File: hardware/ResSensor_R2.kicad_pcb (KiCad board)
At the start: 2 copper layers, 36.9 x 17 mm, 33 parts, among them J1 Conn_01x02, J2 Conn_01x04, U1 SPX3819M5-L-3-3, U2 STM32G030F6Px, U3 nRF24L01P, U4 CS1237, Y1 16MHz

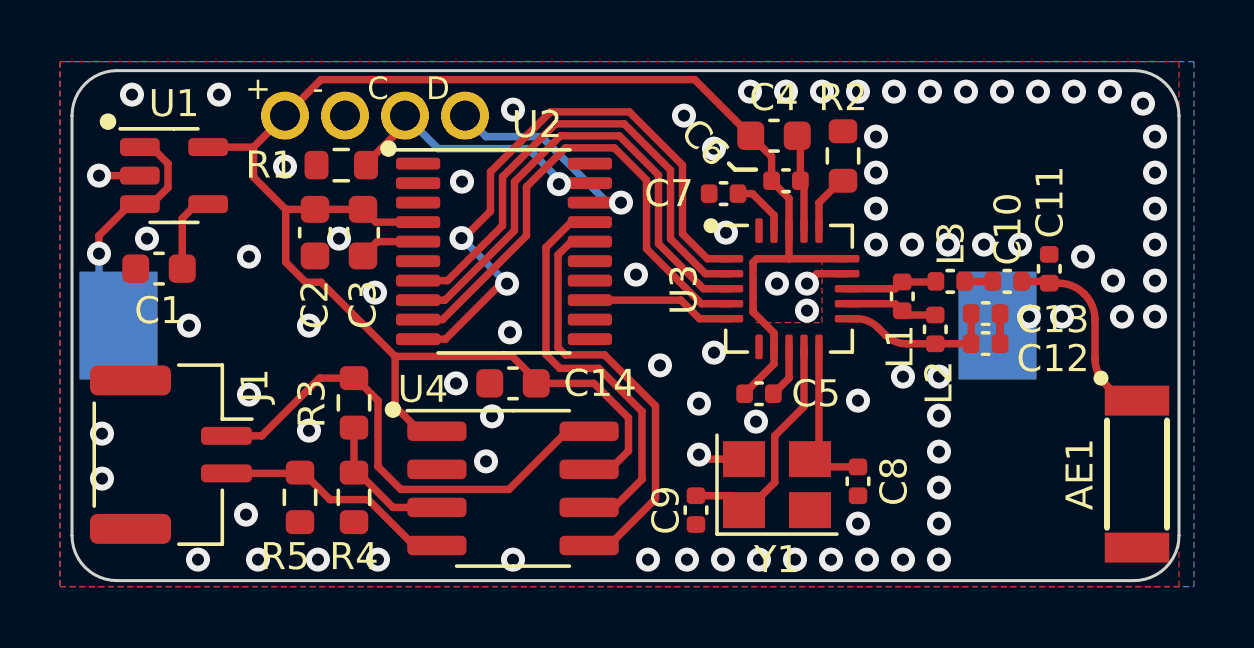
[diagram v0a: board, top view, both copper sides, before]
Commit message: Revise hardware, adding indicator LED
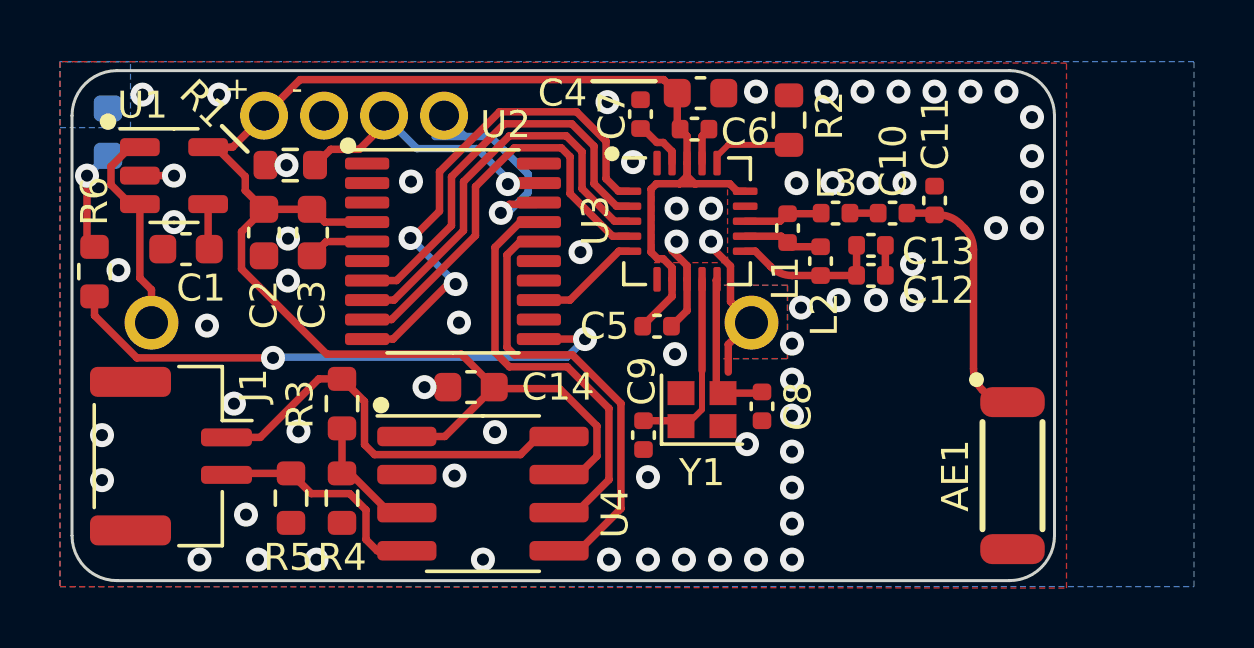
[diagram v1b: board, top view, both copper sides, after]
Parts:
- added D1: Yellow, LED_SMD:LED_0603_1608Metric, B.Cu at (20.4, 20.1)
- added R6: 2k TBD, Resistor_SMD:R_0603_1608Metric, F.Cu at (19.9, 24.7)
- BT1: footprint Battery:BatteryHolder_Keystone_1060_1x2032 -> ResSensor_footprints:BatteryHolder_2032_THT_P20
- Y1: footprint Crystal:Crystal_SMD_3225-4Pin_3.2x2.5mm -> Crystal:Crystal_SMD_2016-4Pin_2.0x1.6mm
- moved C11 4.45 mm to (48.0, 22.3)
- moved C12 4.45 mm to (45.8, 24.8)
- moved C13 4.45 mm to (45.8, 23.8)
- moved C10 4.45 mm to (46.6, 22.8)
- moved L1 4.45 mm to (43.1, 23.2)
- moved L2 4.45 mm to (44.2, 24.4)
- moved L3 4.45 mm to (44.7, 22.8)
- moved AE1 4.15 mm to (50.5, 31.5)
- moved C5 4.08 mm to (38.7, 26.5)
- moved U3 4.08 mm to (39.7, 23.0)
- moved C8 4.06 mm to (42.2, 29.2)
- moved C7 3.83 mm to (38.1, 19.4), turned to 90 degrees
- moved G*** 3.70 mm to (45.5, 32.7)
- moved G*** 3.70 mm to (45.7, 20.4)
- moved Y1 3.54 mm to (40.2, 29.3)
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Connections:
- U2 pad 11: unconnected-(U2-PA4-Pad11) -> LED_ACT
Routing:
- net LED_ACT: track 0.00 -> 19.4 mm, vias 0 -> 2
- net VDD: track 61.3 -> 57.7 mm
- net nRF_CE: track 20.7 -> 17.5 mm
- net SPI1_CK: track 17.1 -> 13.9 mm
- net SPI1_MOSI: track 17.2 -> 14.0 mm
- net SPI1_CSx: track 17.0 -> 13.7 mm
- net Net-(D1-A): track 0.00 -> 3.19 mm, vias 0 -> 1
- net Net-(J1-Pin_1): track 16.5 -> 13.5 mm
- net Net-(U3-XC2): track 8.13 -> 6.55 mm
- net Net-(AE1-FEED): track 7.24 -> 8.82 mm
- net SPI1_MISO: track 4.96 -> 3.68 mm
- net GND: track 12.5 -> 13.7 mm, vias 86 -> 66
- net Net-(BT1-+): track 8.28 -> 7.18 mm, vias 1 -> 0
- net Net-(U1-BP): track 2.73 -> 1.90 mm
- net ADC_CK: track 14.3 -> 15.1 mm
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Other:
- board size 36.9 x 17 mm -> 32.8 x 17 mm
- board text added: "Resistance Telemetry"
- board text added: "Rev. 2a 2023.12"
- board text removed: "Rev. 2 2023.11"
- board text removed: "Var. Res. Remote Coll."

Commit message: Update firmware with blinking LED
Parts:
- R3, R4: value 8.2k -> 4.99k
- R5: value 1.2k -> 4.99k
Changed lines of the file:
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@@
         (effects (font (size 0.9 0.9) (thickness 0.15)))
     )
-    (fp_text value "8.2k" (at 0 1.43 90) (layer "F.Fab")
+    (fp_text value "4.99k" (at 0 1.43 90) (layer "F.Fab")
         (effects (font (size 1 1) (thickness 0.15)))
     )
@@
         (effects (font (size 0.9 0.9) (thickness 0.15)))
     )
-    (fp_text value "8.2k" (at 0 1.43 90) (layer "F.Fab")
+    (fp_text value "4.99k" (at 0 1.43 90) (layer "F.Fab")
         (effects (font (size 1 1) (thickness 0.15)))
     )
@@
         (effects (font (size 0.9 0.9) (thickness 0.15)))
     )
-    (fp_text value "1.2k" (at 0 1.43 90) (layer "F.Fab")
-        (effects (font (size 1 1) (thickness 0.15)))
-    )
+    (fp_text value "4.99k" (at 0 1.43 90) (layer "F.Fab")
+        (effects (font (size 1 1) (thickness 0.15)))
+    )
